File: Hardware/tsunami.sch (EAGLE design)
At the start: 157 parts, among them J1 VDC-IN, J10 TRIG2, J11 TRIG1, J12 USD-SDIO-SOCKET, J13 GND, J14 AUDIO I/O, J15 MIDI, J2 GND-IN, J3 DEBUG, J4 USB-MICROB", J5 CORTEX_DEBUGPTH, J6 3.3VA, J7 3.3V, J8 PLAYING, J9 FTDI_DEVICE, Q1 2.5A/30V, U1 LM1117, U2 LM1117, U3 ATSAMS70N20A-AN, U4 AK4618VQ, U5 74AHC1G125, U6 6N138M, Y1 11.2896 MHz

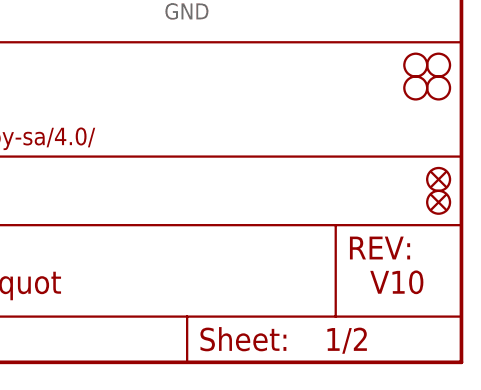
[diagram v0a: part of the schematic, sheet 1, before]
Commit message: Fixing silkscreen labels on panel.
Transposed 2 and 5 labels on MIDI out port.
Rolled version to V11 on all files.
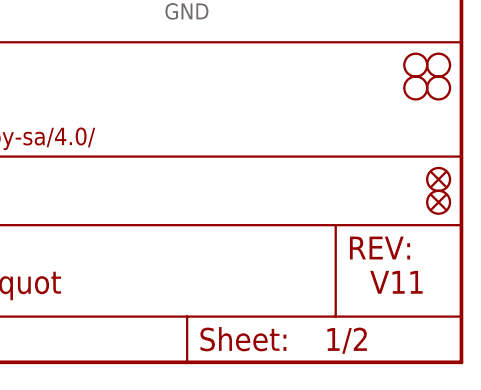
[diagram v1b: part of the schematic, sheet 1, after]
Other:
- note added: "V11"
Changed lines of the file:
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@@
 <?xml version="1.0" encoding="utf-8"?>
 <!DOCTYPE eagle SYSTEM "eagle.dtd">
-<eagle version="7.5.0">
+<eagle version="7.7.0">
 <drawing>
 <settings>
@@
 <wire x1="431.8" y1="119.38" x2="330.2" y2="119.38" width="0.1524" layer="97" style="shortdash"/>
 <text x="335.28" y="7.62" size="2.54" layer="94" font="vector">Jamie Robertson &amp; Byron Jacquot</text>
-<text x="421.64" y="7.62" size="2.54" layer="94" font="vector">V10</text>
+<text x="421.64" y="7.62" size="2.54" layer="94" font="vector">V11</text>
 <text x="249.428" y="236.728" size="1.778" layer="97">Near each VDDCORE pin</text>
 <text x="216.408" y="236.728" size="1.778" layer="97">Near each VDDIO pin</text>
